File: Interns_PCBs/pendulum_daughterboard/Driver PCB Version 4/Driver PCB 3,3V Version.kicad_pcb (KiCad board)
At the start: 2 copper layers, 67 parts, among them IC5 MAX9928FAUA+, J1 AVR-ISP-6, J2 Coil, J3 DRIVE_5V, J4 Conn_01x04, J5 DRIVE_GND, Q1 BC858W, Q2 BD911, SW1 SW_Push, U1 4081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

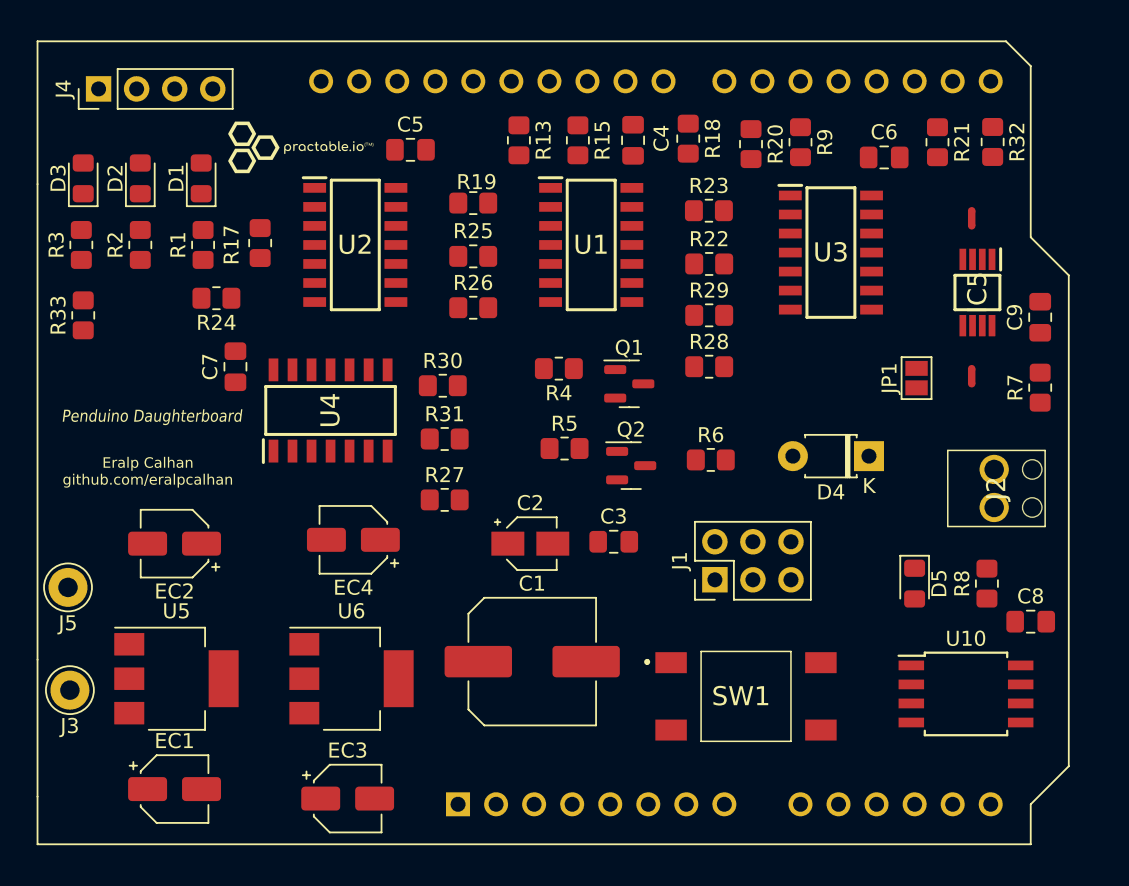
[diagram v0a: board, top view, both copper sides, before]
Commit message: 3.3V PCB Design
PCB with 2 voltage regulators, regulating both the 5V input from the digital pins and the external 5V from the terminal block.
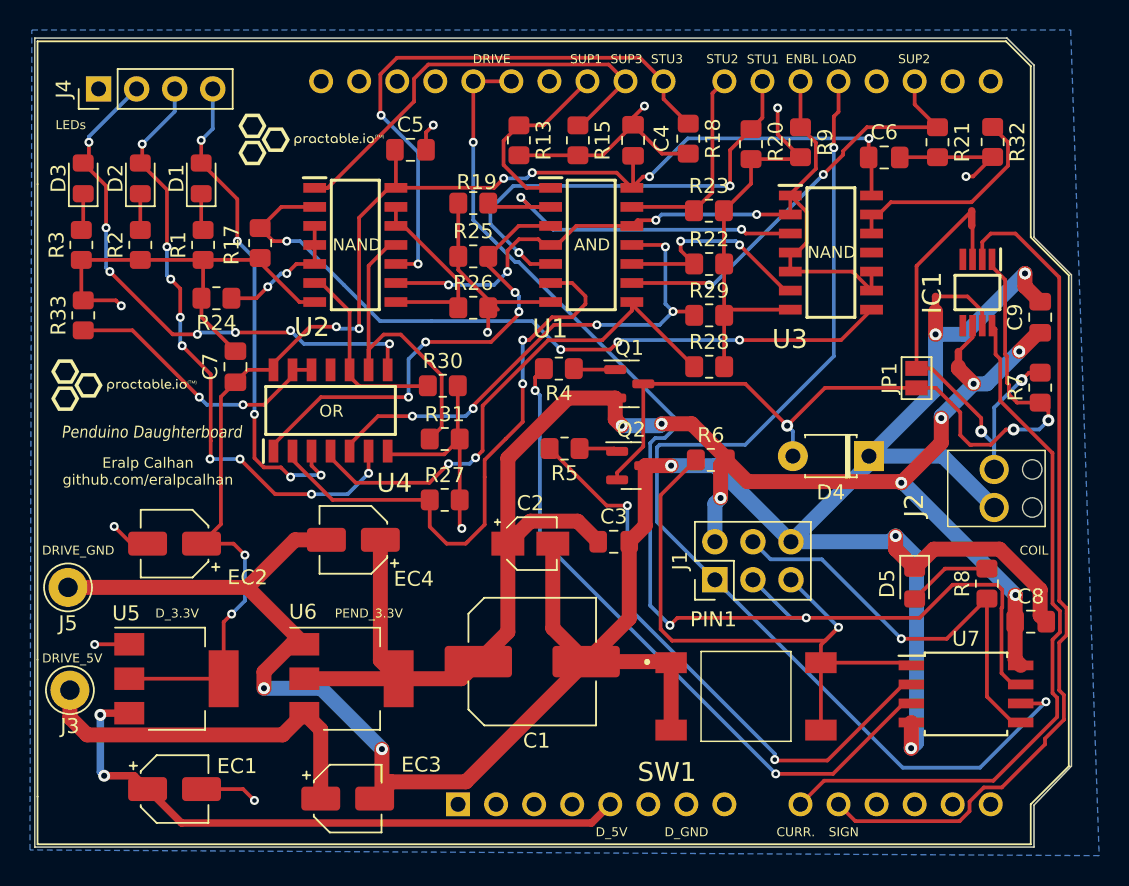
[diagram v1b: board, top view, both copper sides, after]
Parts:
- added G***: LOGO, 000_Graphics_Immo:practactable.io_text_10x4, F.Cu at (109.6, 86.1)
- added NT3: NetTie_2, NetTie:NetTie-2_SMD_Pad0.5mm, F.Cu at (163.8, 80.6)
- moved NT2 1.45 mm to (165.4, 84.3), turned to -90 degrees
- moved G*** 0.87 mm to (122.1, 69.7)
- turned NT1 to -90 degrees
- turned R5 to 180 degrees
- renumbered IC5 to IC1, U10 to U7
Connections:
- IC1 pad 7: DRIVE_GND -> Net-(IC1-Pad7)
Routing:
- net DRIVE_GND: track 0.00 -> 182.9 mm, vias 0 -> 7
- net D_GND: track 0.00 -> 118.9 mm, vias 0 -> 10
- net PEND_3.3V: track 0.00 -> 112.1 mm, vias 0 -> 8
- net D_3.3V: track 0.00 -> 93.3 mm, vias 0 -> 8
- net DRIVE_INPUT: track 0.00 -> 81.4 mm, vias 0 -> 3
- net LOAD_INPUT: track 0.00 -> 74.1 mm, vias 0 -> 2
- net CURRENT_SIGN_OUT: track 0.00 -> 56.7 mm
- net Net-(IC1-Pad1): track 0.00 -> 54.9 mm, vias 0 -> 3
- net STUDENT_ENABLE: track 0.00 -> 52.9 mm, vias 0 -> 4
- net Net-(R17-Pad1): track 0.00 -> 49.5 mm, vias 0 -> 4
- net CURRENT_SENSE_OUT: track 0.00 -> 47.9 mm
- net DRIVE_OUT: track 0.00 -> 44.9 mm, vias 0 -> 2
- net Net-(J1-Pad5): track 0.00 -> 42.8 mm, vias 0 -> 1
- net D_5V: track 0.00 -> 41.8 mm, vias 0 -> 2
- net Net-(D2-Pad2): track 0.00 -> 41.2 mm, vias 0 -> 9
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- added copper zone on B.Cu, net D_GND
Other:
- board outline added: 69.2 x 54 mm
- board text added: "AND"
- board text added: "COIL"
- board text added: "CURR."
- board text added: "DRIVE"
- board text added: "DRIVE_5V"
- board text added: "DRIVE_GND"
- board text added: "D_3.3V"
- board text added: "D_5V"
- board text added: "D_GND"
- board text added: "ENBL"
- board text added: "LEDs"
- board text added: "LOAD"
- board text added: "NAND"
- board text added: "OR"
- board text added: "PEND_3.3V"
- board text added: "PIN1"
- board text added: "SIGN"
- board text added: "STU1"
- board text added: "STU2"
- board text added: "STU3"
- board text added: "SUP1"
- board text added: "SUP2"
- board text added: "SUP3"
